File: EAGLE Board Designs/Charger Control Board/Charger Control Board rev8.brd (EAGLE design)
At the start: 86.4 x 101.6 mm, 121 parts, among them K1 RELAY_DPDT, K2 RELAY_DPDT, K3 RELAY_DPDT, U1 LOGICGATE_BUFFER, U100 MCP2562FD, U101 MCP2562FD, U2 ADM8316WBX30, U3 VOLTAGE_REGULATOR_MODULE_OKI-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

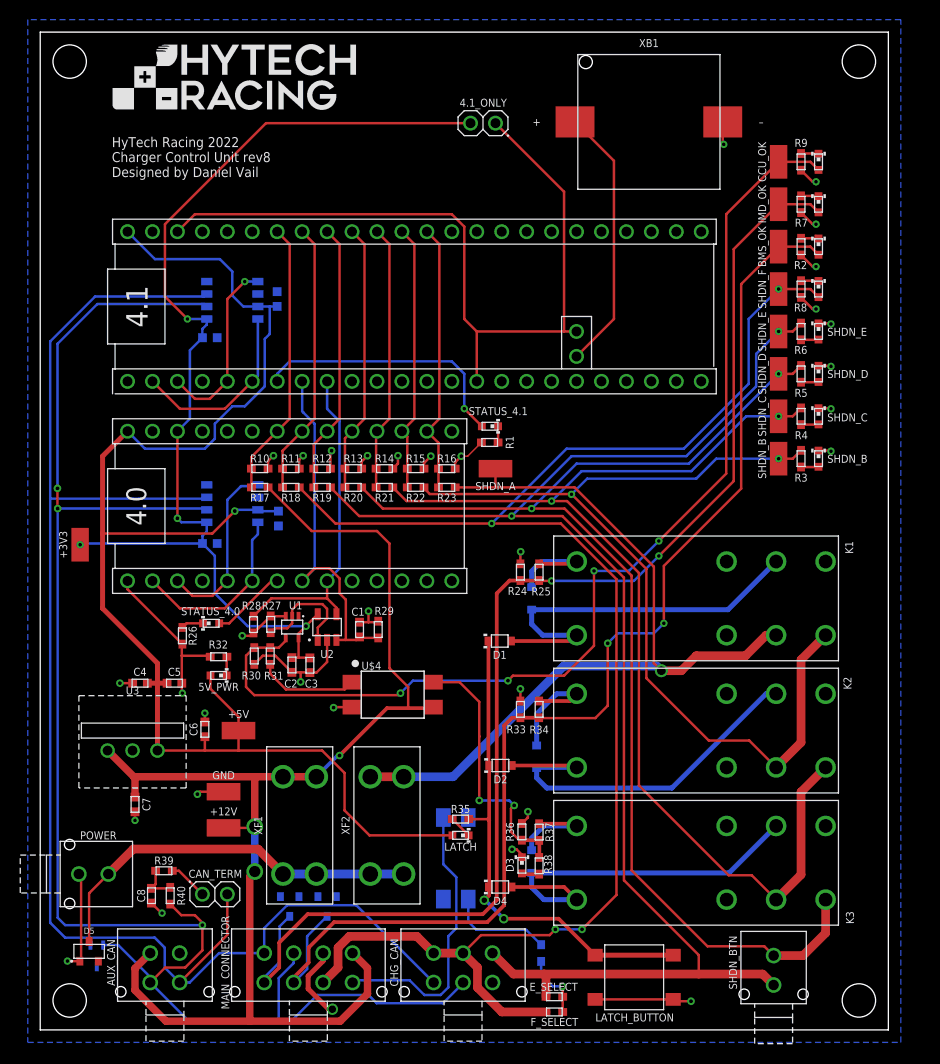
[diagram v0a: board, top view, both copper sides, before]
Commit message: enlarged logo. minor cleaning up.
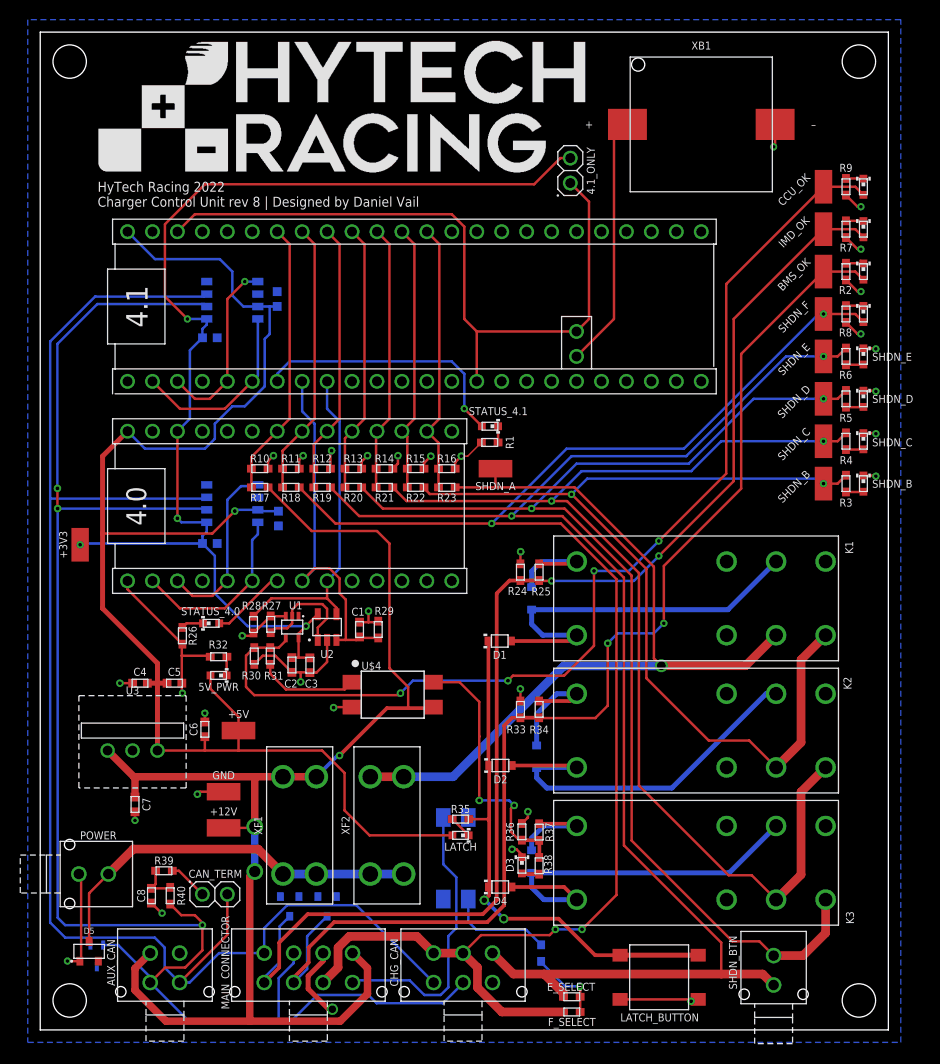
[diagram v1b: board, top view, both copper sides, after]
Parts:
- removed U$5: (no value), HyTechManufacturing:LOGO_HYTECH_MEDIUM
- added U$3: (no value), HyTechManufacturing:LOGO_HYTECH_LARGE
- moved 4.1_ONLY 10.1 mm to (54.0, 87.5), turned to 90 degrees
- moved XB1 5.34 mm to (67.3, 92.2)
- moved R2 5.23 mm to (82.0, 77.2)
- moved R5 5.23 mm to (82.0, 64.3)
- moved R6 5.23 mm to (82.0, 68.6)
- moved R8 5.23 mm to (82.0, 72.9)
- moved TP4 5.23 mm to (79.8, 64.3)
- moved TP5 5.23 mm to (79.8, 68.6)
- moved TP6 5.23 mm to (79.8, 72.9)
- moved TP7 5.23 mm to (79.8, 77.2)
- moved R3 5.23 mm to (82.0, 55.6)
- moved R4 5.23 mm to (82.0, 59.9)
- moved TP2 5.23 mm to (79.8, 55.6)
- moved TP3 5.23 mm to (79.8, 59.9)
- moved R7 5.23 mm to (82.0, 81.5)
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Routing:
- net +3V3: track 111.0 -> 119.7 mm
- net N$36: track 81.0 -> 73.3 mm
- net SHDN_B: track 95.0 -> 99.0 mm
- net SHDN_C: track 114.0 -> 117.5 mm
- net SHDN_E: track 149.1 -> 152.4 mm
- net LATCH_BUTTON: track 50.3 -> 52.8 mm
- net SHDN_D: track 122.4 -> 124.1 mm
- net SHDN_F: track 164.2 -> 165.6 mm
- net N$8: track 27.1 -> 25.8 mm
- net GND: track 109.1 -> 108.0 mm
- net N$5: track 6.65 -> 7.68 mm
- net SHDN_A: track 84.1 -> 83.2 mm
- net IMD_OK: track 131.1 -> 130.4 mm
- net CCU_OK: track 110.1 -> 109.5 mm
- net BMS_OK: track 124.3 -> 123.6 mm
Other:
- board text added: "HyTech Racing 2022 Charger Control Unit rev 8 | Designed by Daniel Vail"
- board text removed: "HyTech Racing 2022 Charger Control Unit rev8 Designed by Daniel Vail"

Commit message: routing cleanup
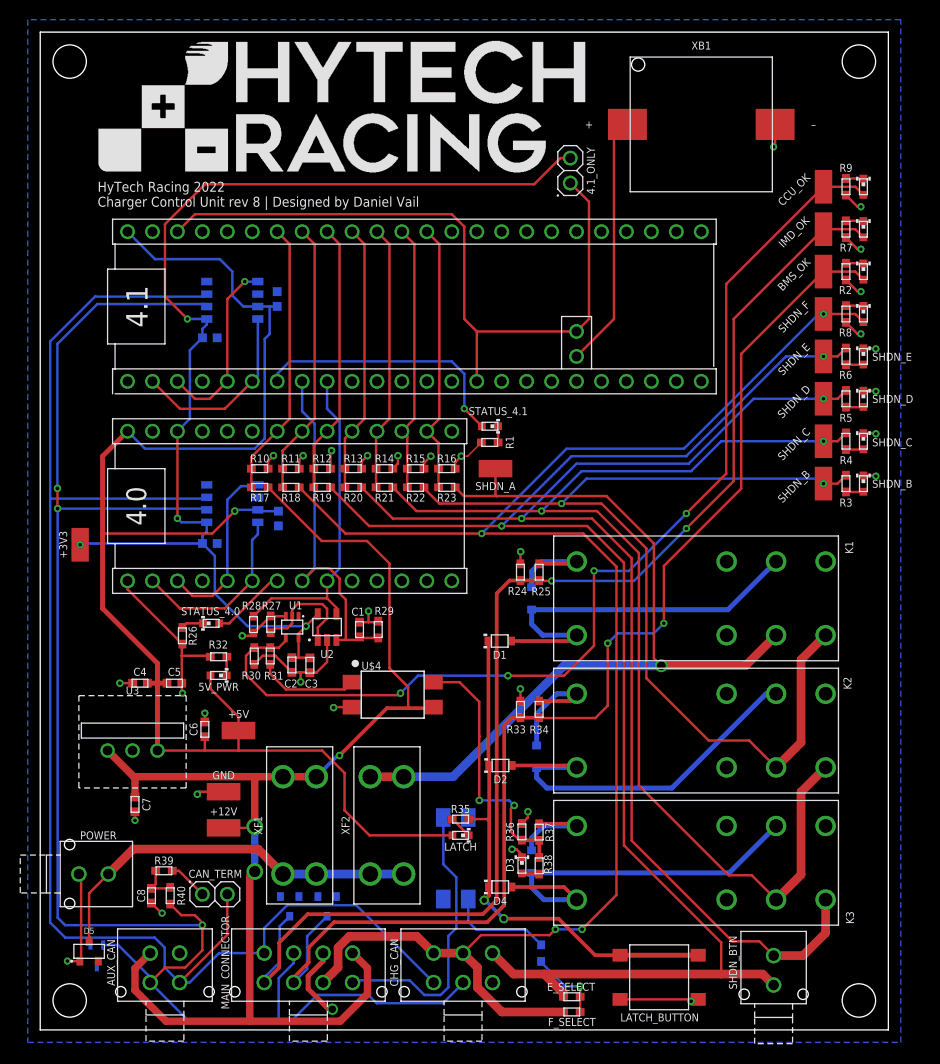
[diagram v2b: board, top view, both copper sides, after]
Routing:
- net SHDN_C: track 117.5 -> 120.1 mm
- net SHDN_B: track 99.0 -> 101.6 mm
- net SHDN_D: track 124.1 -> 126.6 mm
- net SHDN_E: track 152.4 -> 154.7 mm
- net SHDN_A: track 83.2 -> 85.5 mm
- net +5V: track 149.3 -> 151.6 mm
- net SHDN_F: track 165.6 -> 167.8 mm
- net +12V: track 135.4 -> 134.2 mm
- net CCU_OK: track 109.5 -> 108.8 mm

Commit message: rewired CAN as differential pair. relocated some diodes.
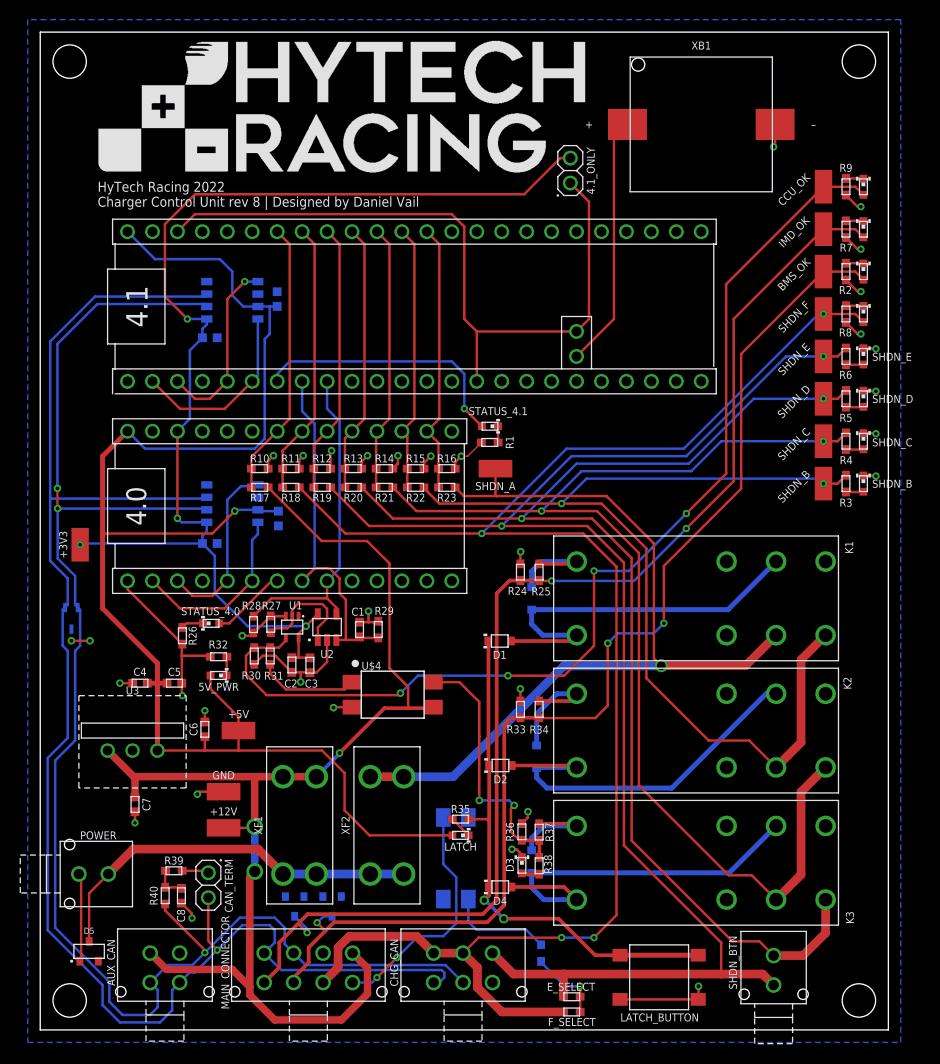
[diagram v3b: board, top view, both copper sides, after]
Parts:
- moved D100 34.5 mm to (3.17, 41.9)
- moved U$10 20.9 mm to (68.6, 91.7), turned to 0 degrees
- moved C8 3.05 mm to (14.4, 13.7)
- moved CAN_TERM 1.13 mm to (17.1, 14.7), turned to 270 degrees
- moved R39 1.02 mm to (13.6, 16.2)
- moved D102 0.51 mm to (25.9, 12.6)
- moved D101 0.51 mm to (29.7, 12.6)
- moved R40 0.51 mm to (12.7, 13.7)
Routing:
- net CANL: track 169.2 -> 157.1 mm
- net +12V: track 134.2 -> 126.7 mm
- net GND: track 108.0 -> 102.9 mm
- net BMS_OK: track 123.6 -> 118.4 mm, vias 2 -> 3
- net RPC_SWITCH: track 29.0 -> 24.4 mm, vias 0 -> 2
- net IMD_OK: track 130.4 -> 126.2 mm, vias 2 -> 3
- net CANH: track 155.6 -> 159.0 mm, vias 0 -> 1
- net N$4: track 4.05 -> 2.74 mm
- net SHDN_F: track 167.8 -> 168.8 mm
- net SHDN_E: track 154.7 -> 153.9 mm
- net CCU_OK: track 108.8 -> 108.2 mm
- net N$9: track 3.91 -> 3.40 mm

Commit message: slight routing
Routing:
- net +12V: track 126.7 -> 125.2 mm
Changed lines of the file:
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@@
 <wire x1="12.8651" y1="6.1595" x2="19.55028125" y2="6.1595" width="0.762" layer="1"/>
 <wire x1="21.336" y1="4.37378125" x2="21.336" y2="3.556" width="0.762" layer="1"/>
-<wire x1="21.336" y1="3.556" x2="23.876" y2="1.016" width="0.762" layer="1"/>
+<wire x1="21.336" y1="3.556" x2="22.098" y2="2.794" width="0.762" layer="1"/>
 <wire x1="11.2014" y1="7.8232" x2="12.8651" y2="6.1595" width="0.762" layer="1"/>
 <wire x1="19.55028125" y1="6.1595" x2="21.336" y2="4.37378125" width="0.762" layer="1"/>
-<wire x1="30.674" y1="1.016" x2="33.3248" y2="3.6668" width="0.762" layer="1"/>
-<wire x1="23.876" y1="1.016" x2="30.674" y2="1.016" width="0.762" layer="1"/>
+<wire x1="32.452" y1="2.794" x2="33.3248" y2="3.6668" width="0.762" layer="1"/>
+<wire x1="22.098" y1="2.794" x2="32.452" y2="2.794" width="0.762" layer="1"/>
 <wire x1="21.336" y1="15.621" x2="21.336" y2="4.37378125" width="0.762" layer="1"/>
 </signal>

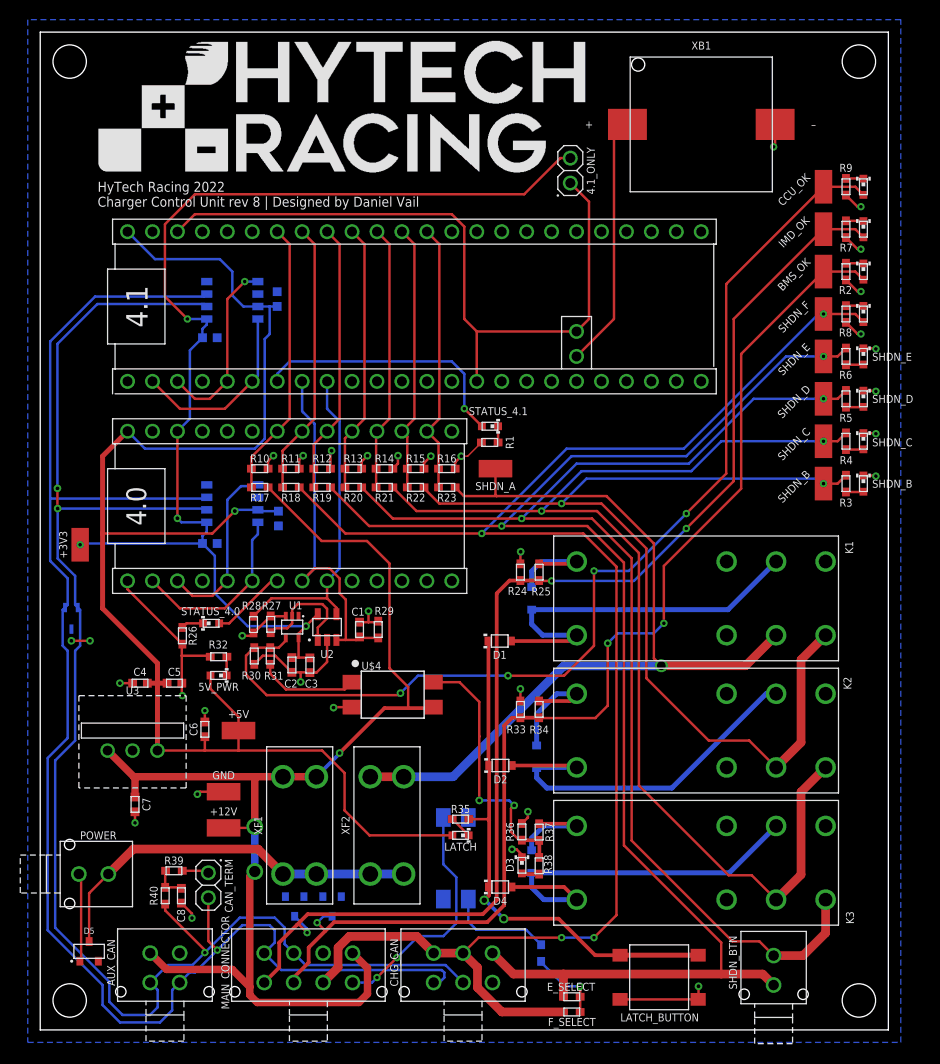
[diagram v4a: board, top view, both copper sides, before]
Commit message: Schematic changes
- Fixed r100 value
- Added latch led pulldown
- Changed 2 pin connectors to horizontal
- Removed second software shdn led
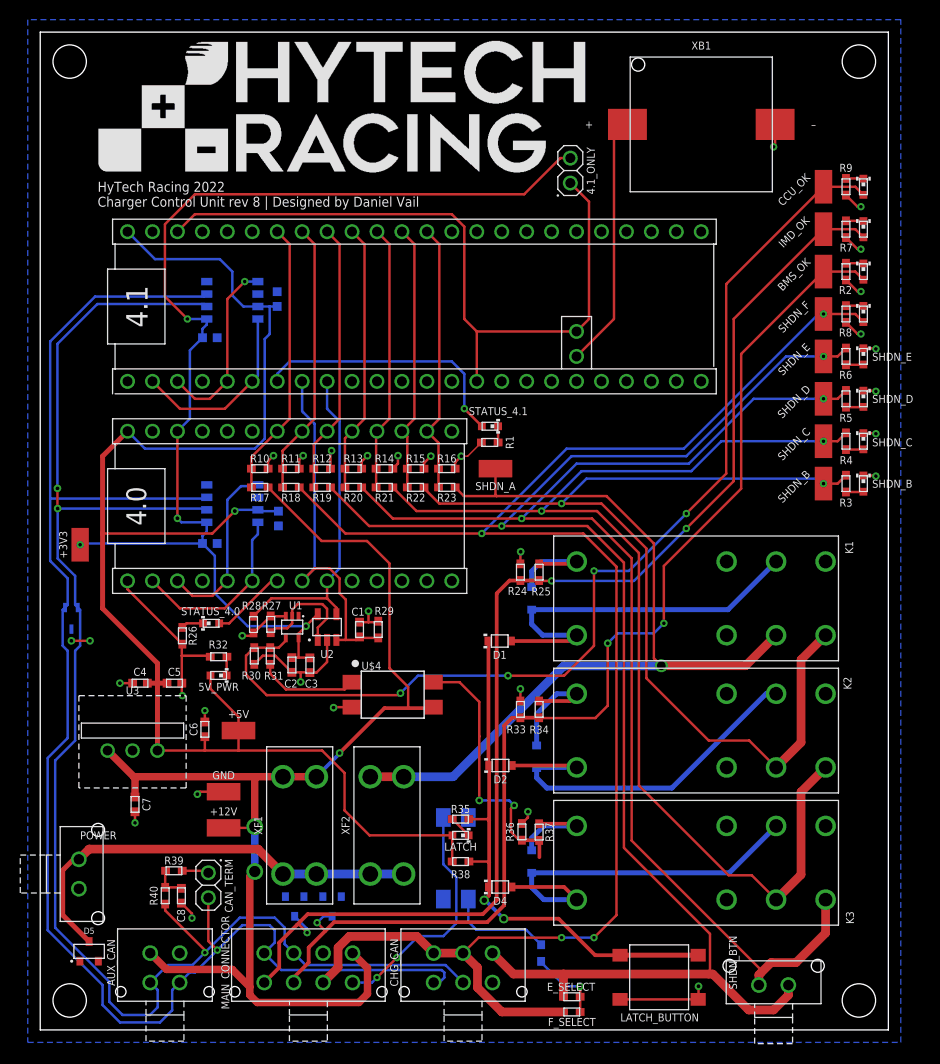
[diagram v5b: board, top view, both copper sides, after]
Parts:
- removed D3: LED_0603_RED, HyTechDevices:0603-LED
- OKHS: value LED_0603_YELLOW -> LED_0603_ORANGE
- POWER, SHDN_BTN: value CONNECTOR-2_μF_T_V_ -> CONNECTOR-2_MF_T_V_; device HyTechDevices:MOLEX_MICROFIT_PTH_VERTICAL_02_DUAL -> HyTechDevices:MOLEX_MICROFIT_PTH_VERTICAL_02_SINGLE
- R100: value RESISTOR_0603_240 -> RESISTOR_0603_1.33K; device HyTechDevices_Jumper:0603-RES -> HyTechDevices:0603-RES
- R38: value RESISTOR_0603_1K -> RESISTOR_0603_10K
- U$100, U$4: device HyTechDevices:DIP-4 -> HyTechDevices_temp:DIP-4
- U2: device HyTechDevices:SOT-23-5 -> HyTechDevices_temp:SOT-23-5
- moved R38 8.01 mm to (42.8, 17.1), turned to 0 degrees
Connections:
- removed net N$21: D3.2, R38.2
- net +5V: now also R38.1
- net GND: no longer D3.1
- net LATCH_BUTTON: now also R38.2
- net N$16: no longer R38.1
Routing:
- net GND: track 102.9 -> 92.5 mm, vias 33 -> 32
- net N$1: track 39.9 -> 45.0 mm
- net SHDN_E: track 153.9 -> 157.7 mm
- net SHDN_D: track 126.6 -> 129.5 mm
- net +5V: track 151.6 -> 154.2 mm
- net LATCH_BUTTON: track 52.8 -> 55.0 mm
- net N$21: track 1.78 -> 0.00 mm

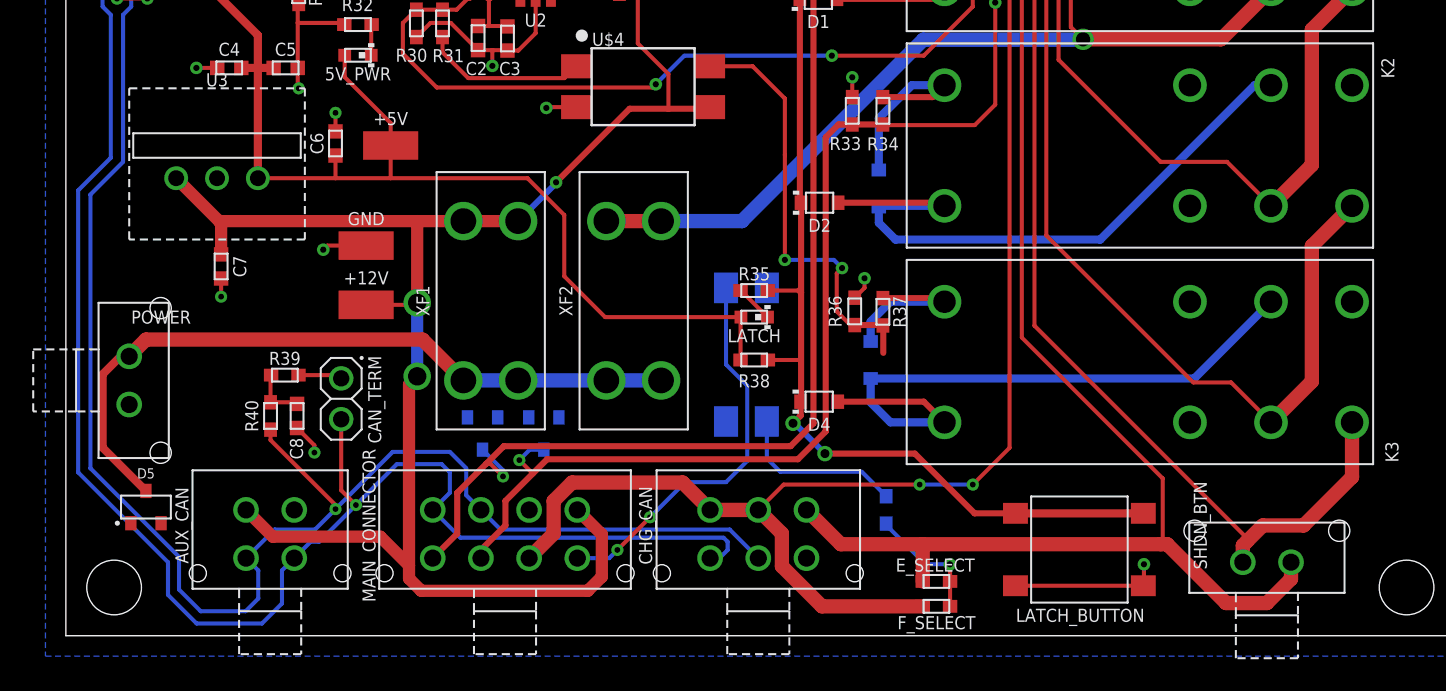
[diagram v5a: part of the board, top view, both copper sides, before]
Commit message: Fixed routing with horizontal 2 pin connectors
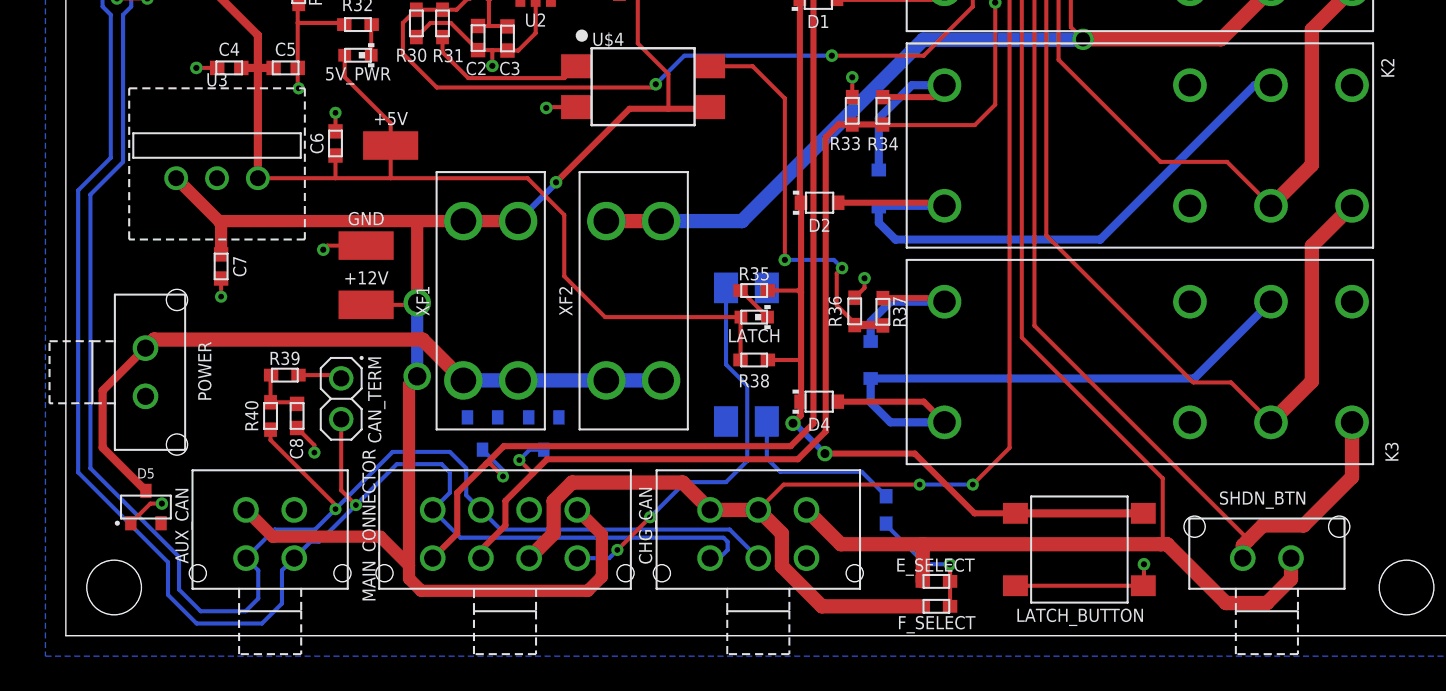
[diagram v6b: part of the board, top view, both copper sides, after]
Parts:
- moved POWER 1.14 mm to (4.95, 16.4)
- moved SHDN_BTN 0.25 mm to (74.7, 4.83)
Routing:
- net GND: track 92.5 -> 94.8 mm, vias 32 -> 33
- net N$16: track 27.1 -> 25.2 mm
- net N$1: track 45.0 -> 44.4 mm
